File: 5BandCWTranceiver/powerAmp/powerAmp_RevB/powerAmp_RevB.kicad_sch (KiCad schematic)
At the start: 52 parts, among them Q6 MOSFET-NCHANNELBS170, T2 2N2222A-SOT223

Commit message: Removed zip files
remove zip files
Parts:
- gave numbers to parts that had none: 4
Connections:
- net GND: now also U$2.11 (V-)
- net VCC12: now also U$2.4 (V+)
- net at C15.1, R13.1: now also U$2.5 (+IN); no longer U$2.3 (+IN)
- net at C14.2, R9.2, U$2.1 (OUT)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: no longer U$2.1 (OUT), U$2.3 (+IN)
- net at R21.1: now also U$2.12 (+IN); no longer U$2.3 (+IN)
- net at R1.2, R14.1: now also U$2.8 (OUT); no longer U$2.1 (OUT)
- net at R14.2, R15.1: now also U$2.9 (-IN); no longer U$2.2 (-IN)
- net at C17.1, R8.1, U$2.3 (+IN): no longer U$2.2 (-IN)
- net at R18.1: now also U$2.14 (OUT); no longer U$2.1 (OUT)
- net at R18.2: now also U$2.13 (-IN); no longer U$2.2 (-IN)
- new net: C18.2, U$2.10 (+IN), U$2.6 (-IN), U$2.7 (OUT)
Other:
- moved on the sheet: C1, C13, C14, C15, C17, C18, C19, C2, C3, C4, C5, C7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

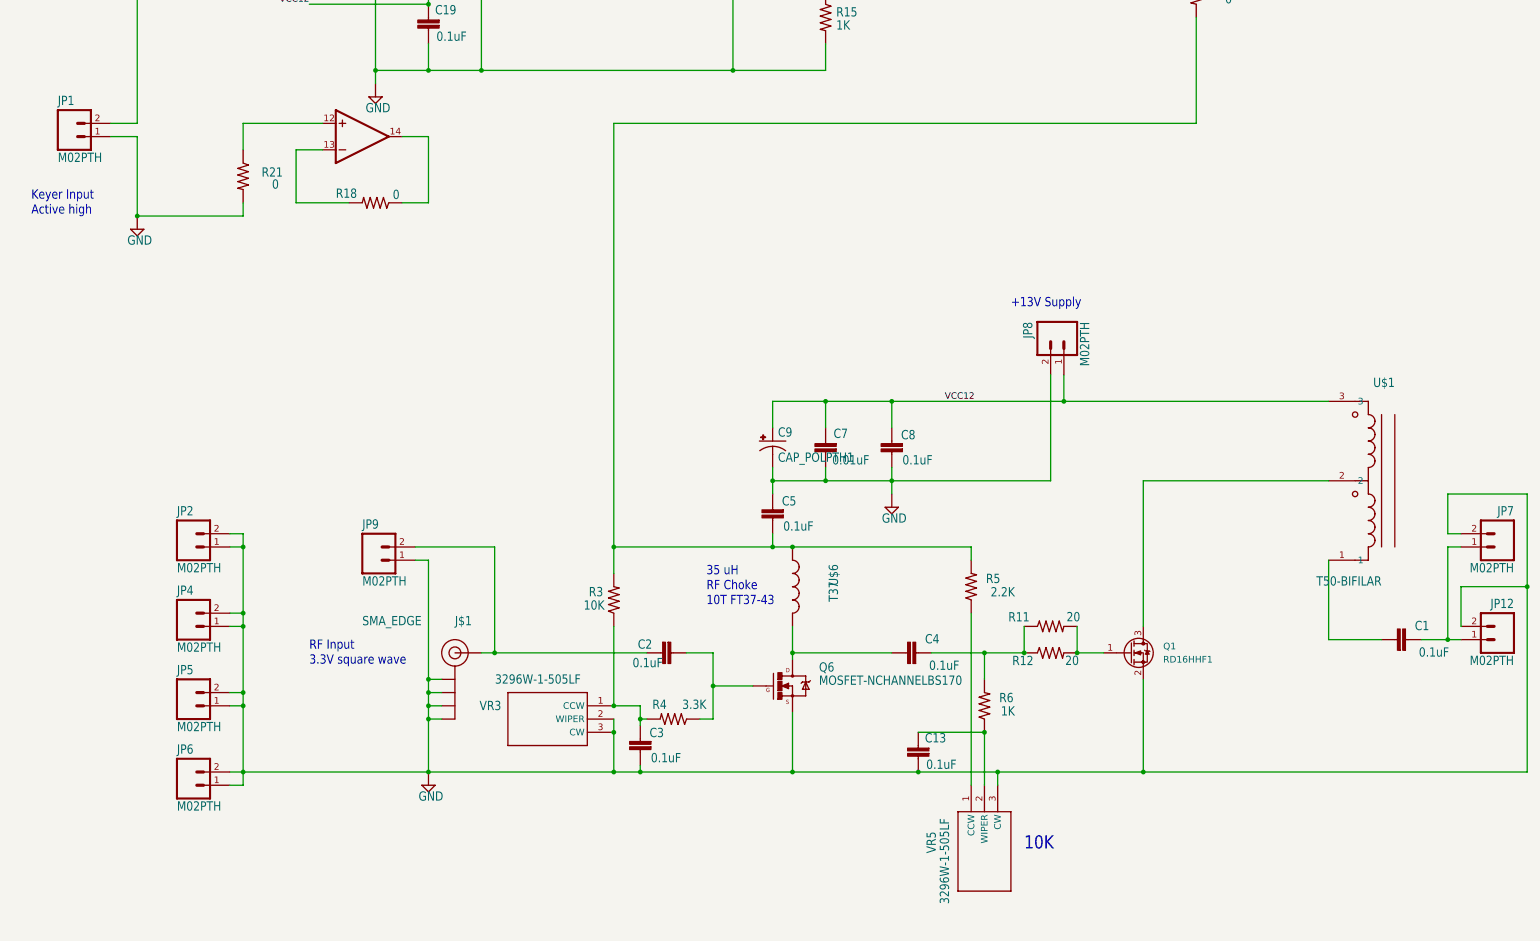
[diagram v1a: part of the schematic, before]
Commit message: Initial completion of schematic and routing
Routing complete; first pass
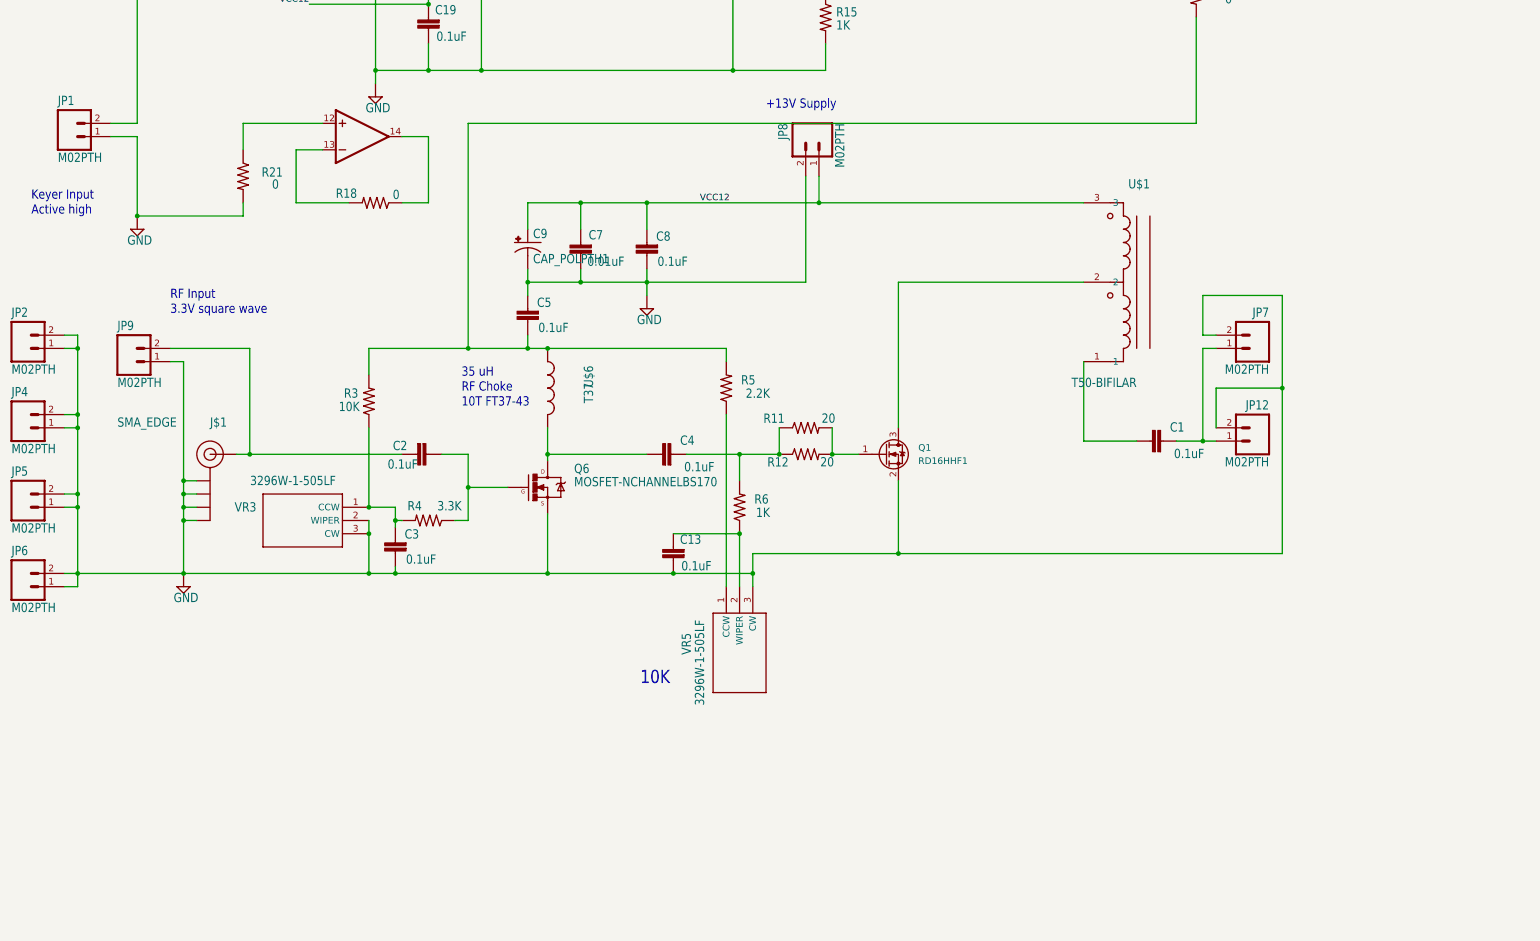
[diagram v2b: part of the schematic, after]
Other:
- moved on the sheet: C1, C13, C2, C3, C4, C5, C7, C8, C9, J$1, JP12, JP2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

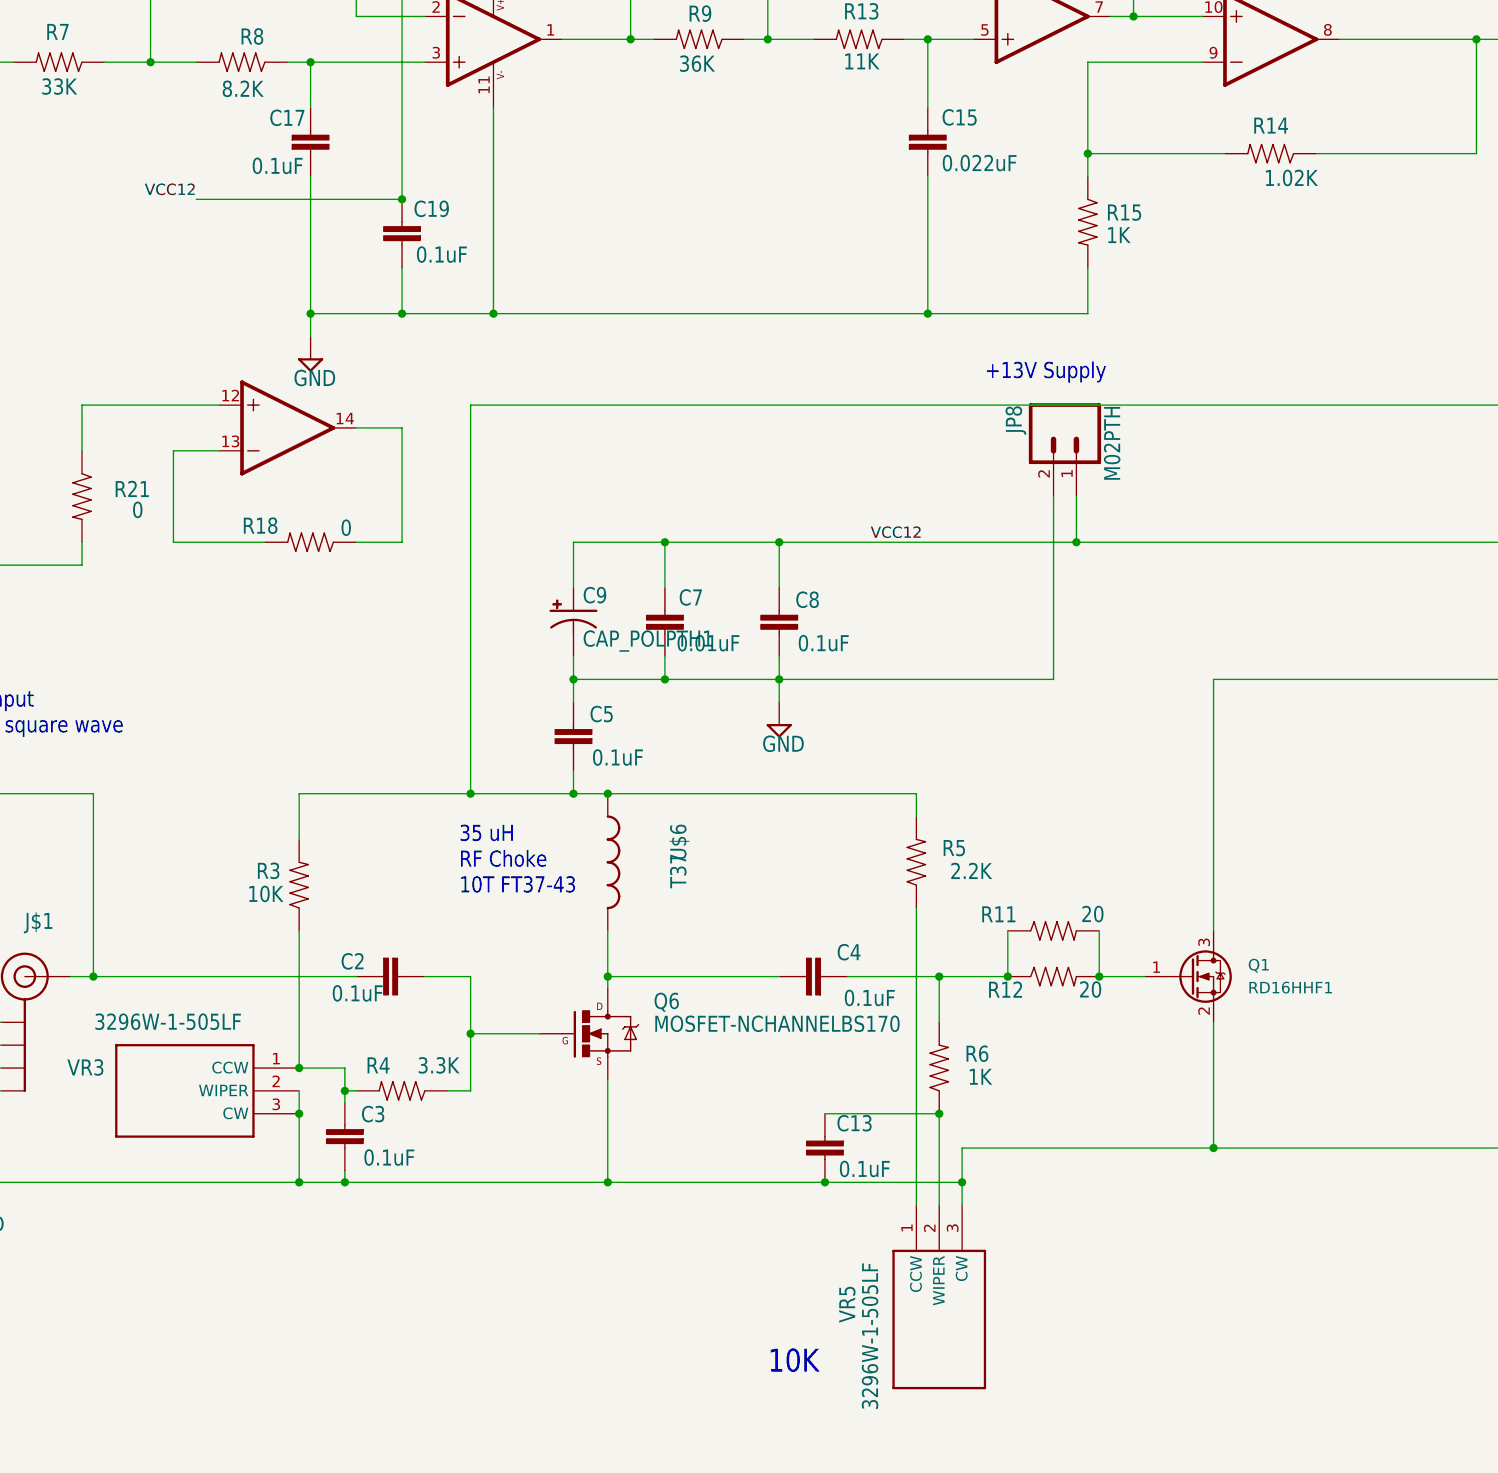
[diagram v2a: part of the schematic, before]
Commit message: Added T/R Switch
Added T/R switch and updated preselector.
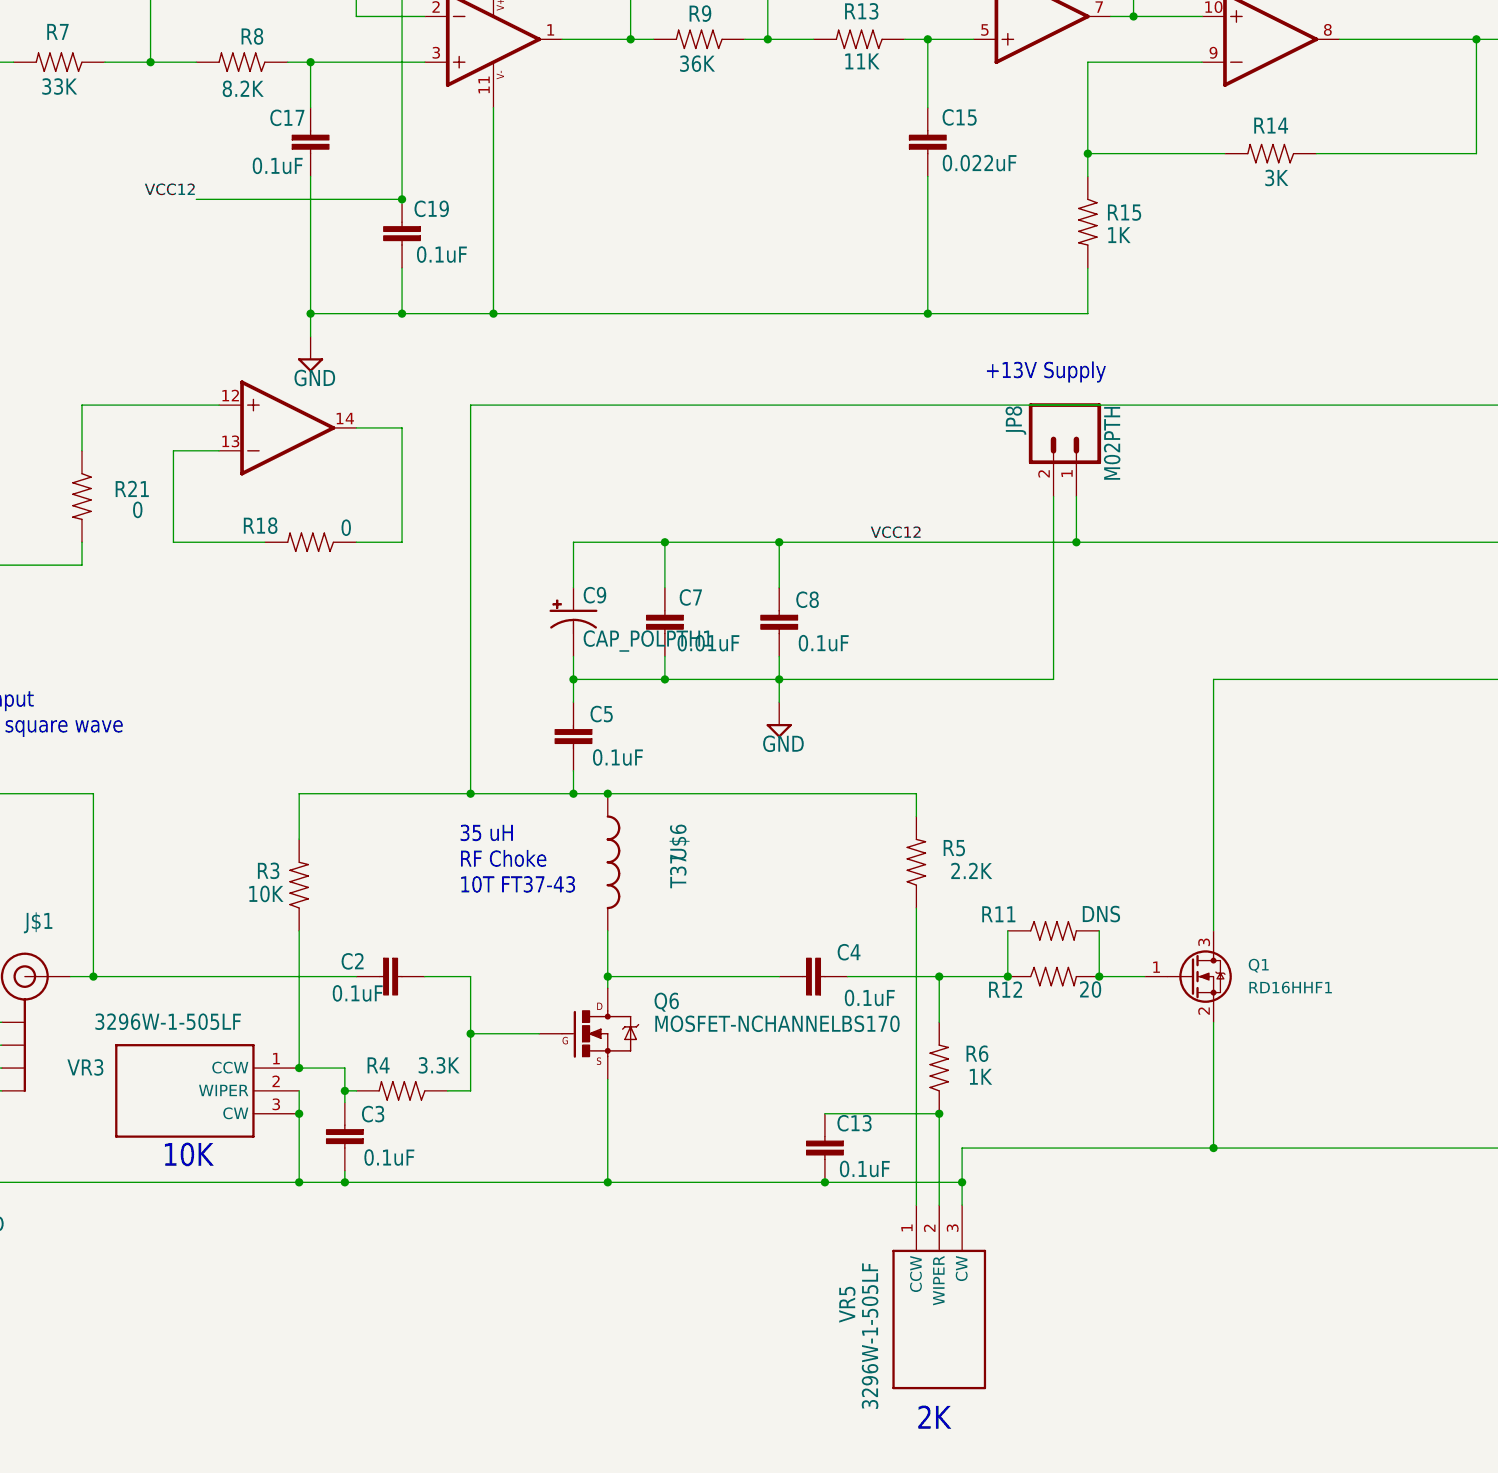
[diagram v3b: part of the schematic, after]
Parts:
- R11: value 20 -> DNS
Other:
- note added: "2K"
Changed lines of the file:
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@@
     (effects (font (size 1.778 1.5113)) (justify left bottom))
+  )
+  (text "10K" (at 66.04 171.45 180)
+    (effects (font (size 2.54 2.159)) (justify left bottom))
   )
   (text "RF Input\n3.3V square wave" (at 43.18 123.19 180)
     (effects (font (size 1.778 1.5113)) (justify left bottom))
   )
-  (text "10K" (at 133.35 194.31 180)
+  (text "2K" (at 149.86 200.66 180)
     (effects (font (size 2.54 2.159)) (justify left bottom))
   )
@@
       (effects (font (size 1.778 1.5113)) (justify left bottom))
     )
-    (property "Value" "20" (id 1) (at 168.148 144.018 0)
+    (property "Value" "DNS" (id 1) (at 168.148 144.018 0)
       (effects (font (size 1.778 1.5113)) (justify left bottom))
     )
@@
       (effects (font (size 1.778 1.5113)) (justify right top))
     )
-    (property "Value" "1.02K" (id 1) (at 188.468 62.23 0)
+    (property "Value" "3K" (id 1) (at 188.468 62.23 0)
       (effects (font (size 1.778 1.5113)) (justify right top))
     )
@@
     )
     (path "/646cbadb-b1e3-4f3d-b836-1d0a4642fad3"
-      (reference "R11") (unit 1) (value "20") (footprint "powerAmp_RevB:1206")
+      (reference "R11") (unit 1) (value "DNS") (footprint "powerAmp_RevB:1206")
     )
     (path "/2cde09e2-1478-4e90-84f2-de808fbc4e00"
@@
     )
     (path "/d9bcd9a9-a340-401d-98c0-3844ecd370f3"
-      (reference "R14") (unit 1) (value "1.02K") (footprint "powerAmp_RevB:0603-RES")
+      (reference "R14") (unit 1) (value "3K") (footprint "powerAmp_RevB:0603-RES")
     )
     (path "/ba105837-9e06-4662-9965-7593b1cae8d0"

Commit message: Updated schematics and layout
Updated T/R switch to rev. B after lab tests
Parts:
- removed R11: DNS, powerAmp_RevB:1206, symbol powerAmp_RevB-eagle-import:RESISTOR1206
- added C10: 1000pF, powerAmp_RevB:CAP-PTH-5MM, symbol powerAmp_RevB-eagle-import:CAPPTH1
- added C6: 0.1uF, powerAmp_RevB:CAP-PTH-5MM, symbol powerAmp_RevB-eagle-import:CAPPTH1
- added R10: 1K, powerAmp_RevB:1206, symbol powerAmp_RevB-eagle-import:RESISTOR1206
- R12: value 20 -> 26.1
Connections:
- net GND: now also C10.1
- net at Q1.1 (G), R12.2: now also R10.1
- net at Q1.3 (D), U$1.2: now also C10.2, C6.2
- new net: C6.1, R10.2
